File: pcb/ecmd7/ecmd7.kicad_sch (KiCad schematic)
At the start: 0 parts

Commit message: WIP: Add supply
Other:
- added sheet Supply (Supply.kicad_sch)
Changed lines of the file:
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@@
+		)
+	)
+	(sheet
+		(at 110.49 46.99)
+		(size 22.86 21.59)
+		(exclude_from_sim no)
+		(in_bom yes)
+		(on_board yes)
+		(dnp no)
+		(fields_autoplaced yes)
+		(stroke
+			(width 0.1524)
+			(type solid)
+		)
+		(fill
+			(color 0 0 0 0.0000)
+		)
+		(property "Sheetname" "Supply"
+			(at 110.49 46.2784 0)
+			(effects
+				(font
+					(size 1.27 1.27)
+				)
+				(justify left bottom)
+			)
+		)
+		(property "Sheetfile" "Supply.kicad_sch"
+			(at 110.49 69.1646 0)
+			(effects
+				(font
+					(size 1.27 1.27)
+				)
+				(justify left top)
+			)
+		)
+		(instances
+			(project "ecmd7"
+				(path "/e730e626-b0ba-4026-9c00-58e2460691fe"
+					(page "4")
+				)
+			)
 		)
 	)

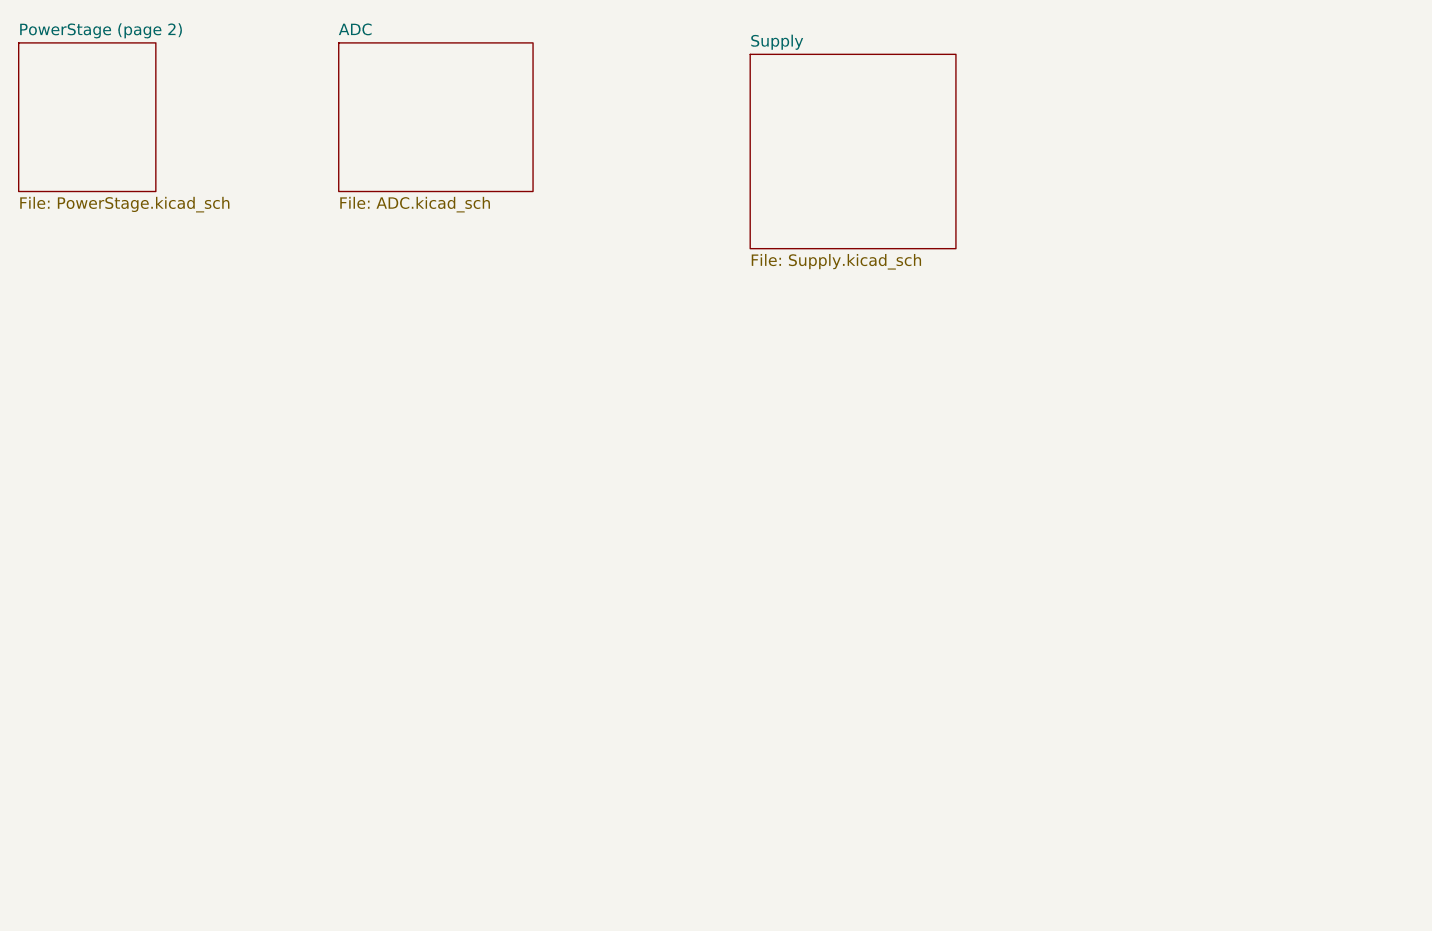
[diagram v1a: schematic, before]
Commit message: WIP: Add ADC inputs
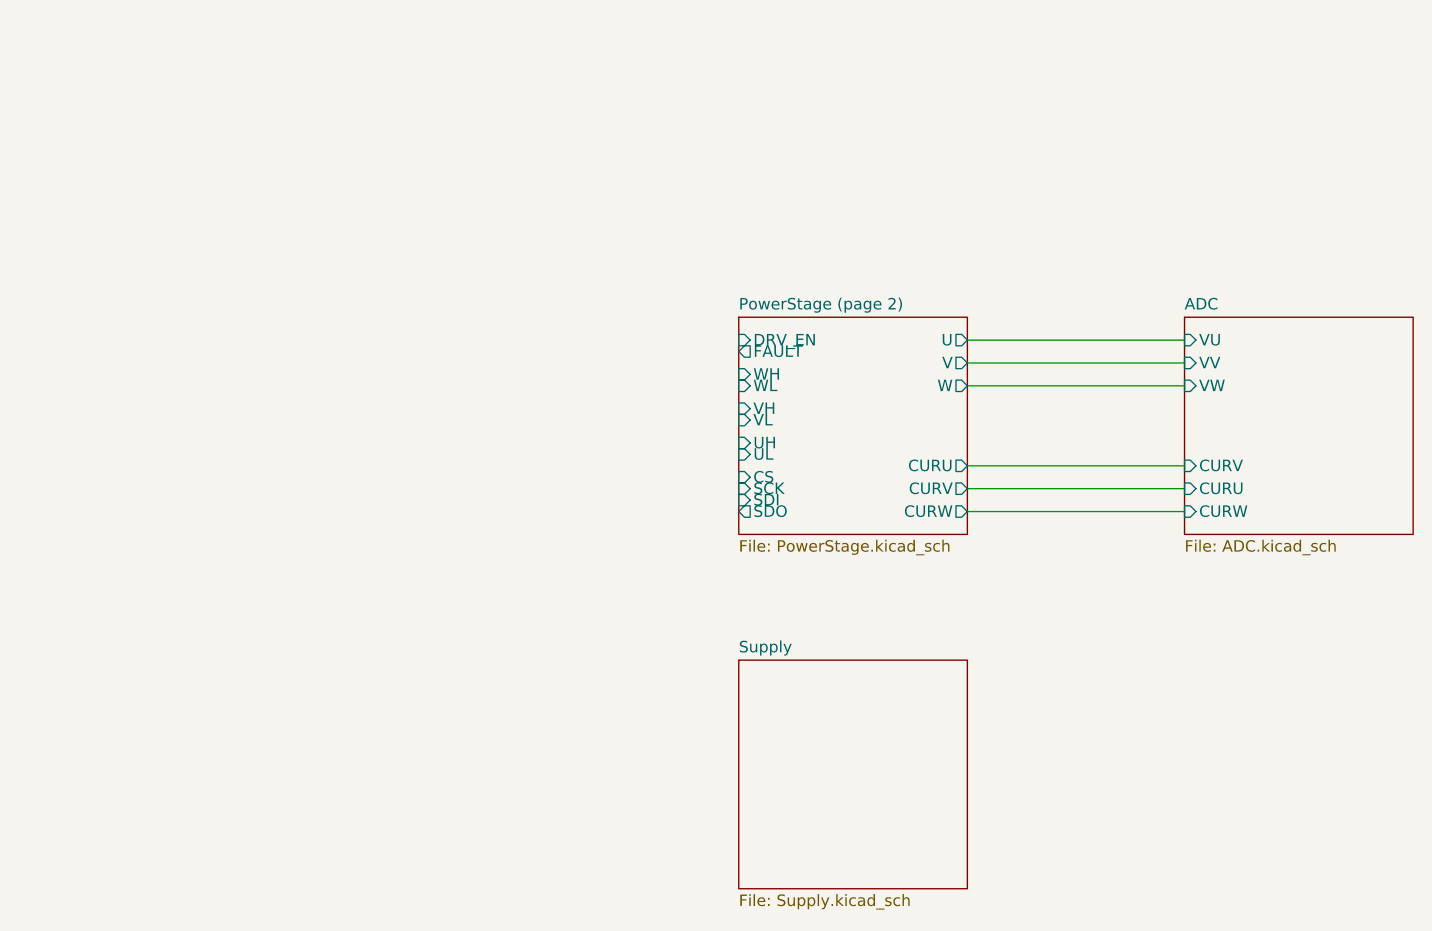
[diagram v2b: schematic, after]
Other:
- sheet ADC ports: added CURU, CURV, CURW, VU, VV, VW; removed none
- sheet PowerStage (page 2) ports: added CS, CURU, CURV, CURW, DRV_EN, FAULT, SCK, SDI, SDO, U, UH, UL, V, VH, VL, W, WH, WL; removed none

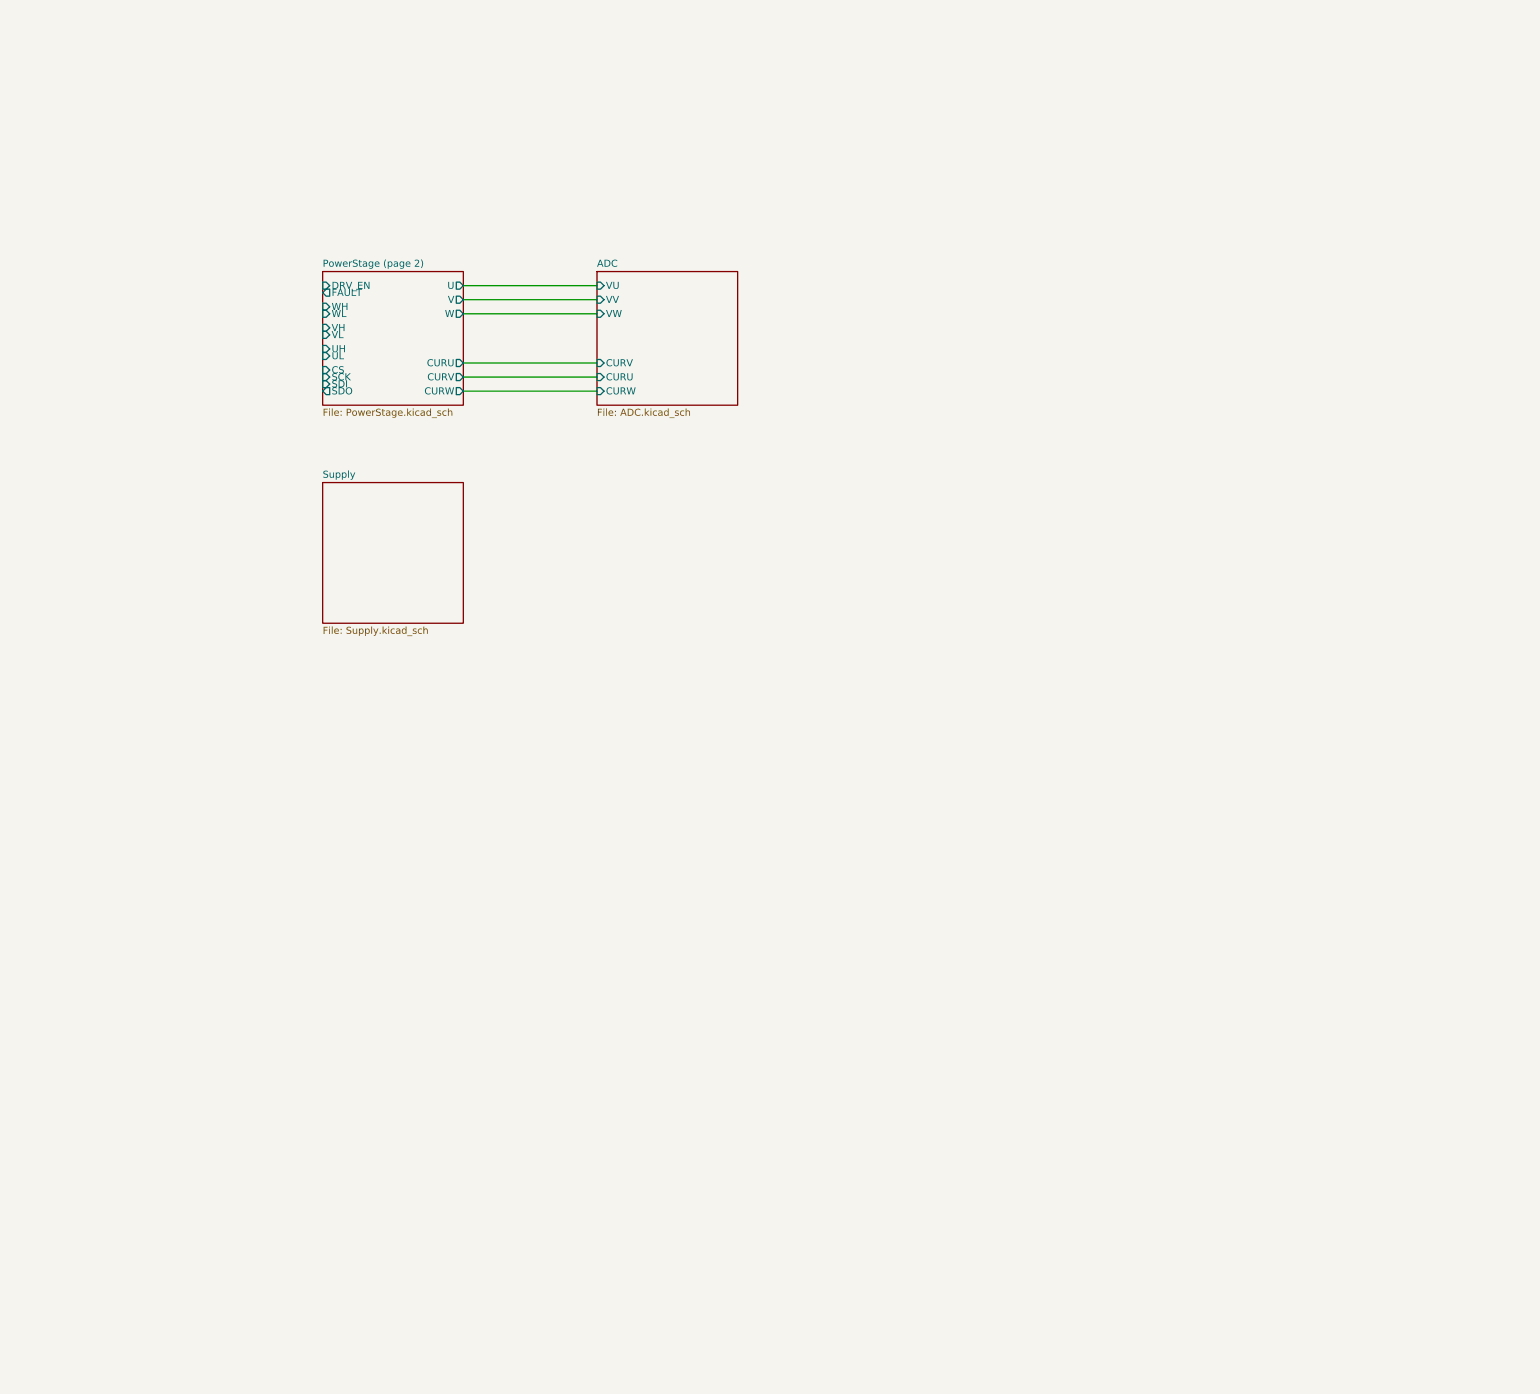
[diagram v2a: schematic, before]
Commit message: WIP: Add sensor interface Re-partition schematic
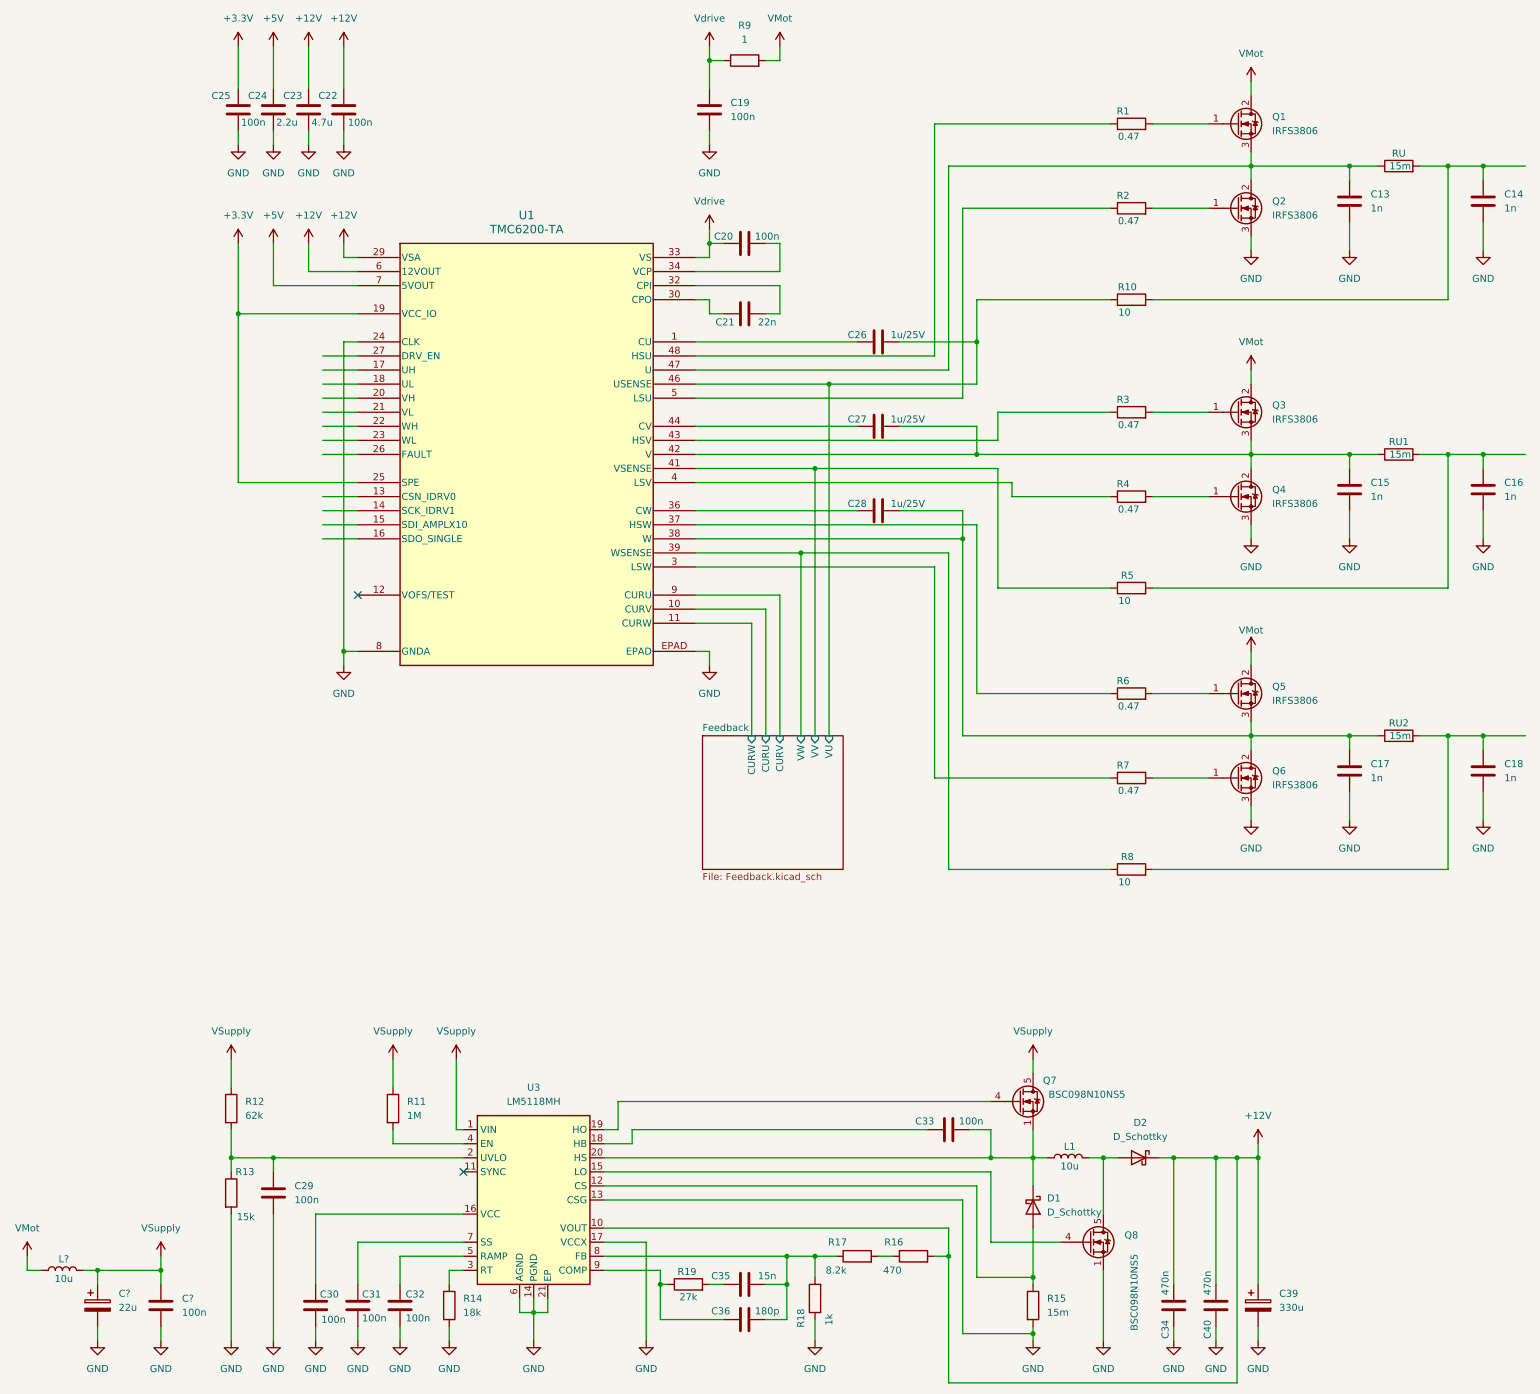
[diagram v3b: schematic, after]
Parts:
- added C13, C14, C15, C16, C17, C18: 1n, Capacitor_SMD:C_0805_2012Metric, symbol Device:C
- added C19, C20, C22, C25: 100n, Capacitor_SMD:C_0805_2012Metric, symbol Device:C
- added C21: 22n, Capacitor_SMD:C_0805_2012Metric, symbol Device:C
- added C23: 4.7u, Capacitor_SMD:C_0805_2012Metric, symbol Device:C
- added C24: 2.2u, Capacitor_SMD:C_0805_2012Metric, symbol Device:C
- added C26, C27, C28: 1u/25V, Capacitor_SMD:C_0805_2012Metric, symbol Device:C
- added C29, C30, C31, C32, C33, C?: 100n, symbol Device:C
- added C34, C40: 470n, symbol Device:C
- added C35: 15n, symbol Device:C
- added C36: 180p, symbol Device:C
- added C39: 330u, Capacitor_SMD:CP_Elec_6.3x9.9, symbol Device:C_Polarized
- added C?: 22u, Capacitor_SMD:CP_Elec_6.3x9.9, symbol Device:C_Polarized
- added D1, D2: D_Schottky, symbol Device:D_Schottky
- added L1, L?: 10u, Inductor_SMD:L_TechFuse_SL0530, symbol Device:L
- added Q1, Q2, Q3, Q4, Q5, Q6: IRFS3806, Package_TO_SOT_SMD:TO-263-2, symbol Transistor_FET:IRFS4115
- added Q7, Q8: BSC098N10NS5, Package_TO_SOT_SMD:TDSON-8-1, symbol Transistor_FET:BSC098N10NS5
- added R1, R2, R3, R4, R6, R7: 0.47, Resistor_SMD:R_0805_2012Metric, symbol Device:R
- added R10, R5, R8: 10, Resistor_SMD:R_0805_2012Metric, symbol Device:R
- added R11: 1M, Resistor_SMD:R_0805_2012Metric, symbol Device:R
- added R12: 62k, Resistor_SMD:R_0805_2012Metric, symbol Device:R
- added R13: 15k, Resistor_SMD:R_0805_2012Metric, symbol Device:R
- added R14: 18k, Resistor_SMD:R_0805_2012Metric, symbol Device:R
- added R15: 15m, symbol Device:R
- added R16: 470, Resistor_SMD:R_0805_2012Metric, symbol Device:R
- added R17: 8.2k, Resistor_SMD:R_0805_2012Metric, symbol Device:R
- added R18: 1k, Resistor_SMD:R_0805_2012Metric, symbol Device:R
- added R19: 27k, Resistor_SMD:R_0805_2012Metric, symbol Device:R
- added R9: 1, Resistor_SMD:R_0805_2012Metric, symbol Device:R
- added RU, RU1, RU2: 15m, Resistor_SMD:R_0612_1632Metric, symbol Device:R
- added U1: TMC6200-TA, eTQFP48_9x9_TRI, symbol ssta_symbols:TMC6200-TA
- added U3: LM5118MH, Package_SO:Texas_PWP0020A, symbol Regulator_Switching:LM5118MH
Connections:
- net Feedback/CURU: now also U1.10 (CURV)
- net Feedback/CURV: now also U1.9 (CURU)
- net Feedback/CURW: now also U1.11 (CURW)
- net Feedback/VU: now also C26.1, R10.1, U1.46 (USENSE)
- net Feedback/VV: now also R5.1, U1.41 (VSENSE)
- net Feedback/VW: now also R8.1, U1.39 (WSENSE)
- new net: C13.1, Q1.3 (S), Q2.2 (D), RU.1, U1.47 (U)
- new net: C35.2, C36.2, R17.1, R18.2, U3.8 (FB)
- new net: R16.1, R17.2
- new net: C29.1, R12.2, R13.1, U3.2 (UVLO)
- new net: C30.1, U3.16 (VCC)
- new net: R2.1, U1.5 (LSU)
- new net: Q2.1 (G), R2.2
- new net: C17.1, C28.1, Q5.3 (S), Q6.2 (D), RU2.1, U1.38 (W)
- new net: C18.1, R8.2, RU2.2
- new net: C36.1, R19.1, U3.9 (COMP)
- new net: D1.2 (A), R15.1, U3.12 (CS)
- new net: Q8.4 (G), U3.15 (LO)
- new net: C33.1, U3.18 (HB)
- new net: Q7.4 (G), U3.19 (HO)
- new net: C33.2, D1.1 (K), L1.1, Q7.1 (S), Q7.2 (S), Q7.3 (S), U3.20 (HS)
- new net: R14.1, U3.3 (RT)
- new net: R11.2, U3.4 (EN)
- new net: C32.1, U3.5 (RAMP)
- new net: C31.1, U3.7 (SS)
- new net: C21.1, U1.32 (CPI)
- new net: C21.2, U1.30 (CPO)
- new net: C26.2, U1.1 (CU)
- new net: C16.1, R5.2, RU1.2
- new net: C14.1, R10.2, RU.2
- new net: C35.1, R19.2
- new net: R3.1, U1.43 (HSV)
- new net: Q3.1 (G), R3.2
- new net: R7.1, U1.3 (LSW)
- new net: Q6.1 (G), R7.2
- new net: Q1.1 (G), R1.2
- new net: Q4.1 (G), R4.2
- new net: C15.1, C27.1, Q3.3 (S), Q4.2 (D), RU1.1, U1.42 (V)
- new net: D2.2 (A), L1.2, Q8.5 (D)
- new net: C20.1, U1.34 (VCP)
- new net: C28.2, U1.36 (CW)
- new net: R6.1, U1.37 (HSW)
- new net: R4.1, U1.4 (LSV)
- new net: C27.2, U1.44 (CV)
- new net: R1.1, U1.48 (HSU)
- new net: Q5.1 (G), R6.2
- new net +12V: C22.1, C23.1, C34.2, C39.1, C40.2, D2.1 (K), R16.2, U1.29 (VSA), U1.6 (12VOUT), U3.10 (VOUT)
- new net +3.3V: C25.1, U1.19 (VCC_IO), U1.25 (SPE)
- new net +5V: C24.1, U1.7 (5VOUT)
- new net GND: C13.2, C14.2, C15.2, C16.2, C17.2, C18.2, C19.2, C22.2, C23.2, C24.2, C25.2, C29.2, C30.2, C31.2, C32.2, C34.1, C39.2, C40.1, C?.2, C?.2, Q2.3 (S), Q4.3 (S), Q6.3 (S), Q8.1 (S), Q8.2 (S), Q8.3 (S), R13.2, R14.2, R15.2, R18.1, U1.24 (CLK), U1.8 (GNDA), U1.EPAD, U3.13 (CSG), U3.14 (PGND), U3.17 (VCCX), U3.21 (EP), U3.6 (AGND)
- new net VMot: L?.1, Q1.2 (D), Q3.2 (D), Q5.2 (D), R9.2
- new net VSupply: C?.1, C?.1, L?.2, Q7.5 (D), R11.1, R12.1, U3.1 (VIN)
- new net Vdrive: C19.1, C20.2, R9.1, U1.33 (VS)
- no-connect marks 0 -> 2
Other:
- sheet ADC renamed Feedback
- removed sheet PowerStage (page 2)
- removed sheet Supply
- sheet Feedback: file ADC.kicad_sch -> Feedback.kicad_sch
- title: (none) -> ECMD7 Power Converter

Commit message: Finlize schematics
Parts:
- added J1, J2, J3: Conn_02x06_Odd_Even, Connector_PinHeader_1.27mm:PinHeader_2x06_P1.27mm_Horizontal, symbol Connector_Generic:Conn_02x06_Odd_Even
- added J4: Conn_01x02_Socket, Connector_AMASS:AMASS_XT60-F_1x02_P7.20mm_Vertical, symbol Connector:Conn_01x02_Socket
- added J5: DE9_Socket, symbol Connector:DE9_Socket
- added J6: Conn_01x04_Socket, Connector_PinHeader_1.27mm:PinHeader_1x04_P1.27mm_Vertical, symbol Connector:Conn_01x04_Socket
- added JU1, JV1, JW1: Screw_Terminal_01x01, MountingHole:MountingHole_3.2mm_M3_Pad_TopBottom, symbol Connector:Screw_Terminal_01x01
- added R44, R45: 4.7k, Resistor_SMD:R_0805_2012Metric, symbol Device:R
- gave numbers to parts that had none: 3
- renumbered RU to RU3
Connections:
- net +12V: now also J5.4
- net +3.3V: now also J1.1 (Pin_1), J1.2 (Pin_2), J2.1 (Pin_1), J2.2 (Pin_2), J3.1 (Pin_1), J3.2 (Pin_2), J6.2 (Pin_2), R44.1, R45.1
- net GND: now also J1.3 (Pin_3), J1.4 (Pin_4), J2.3 (Pin_3), J2.4 (Pin_4), J3.3 (Pin_3), J3.4 (Pin_4), J4.2 (Pin_2), J5.5, J6.1 (Pin_1)
- net VMot: now also J4.1 (Pin_1)
- net at C18.1, R8.2, RU2.2: now also JW1.1 (Pin_1)
- net at C16.1, R5.2, RU1.2: now also JV1.1 (Pin_1)
- net at C14.1, R10.2, RU3.2: now also JU1.1 (Pin_1)
- net CS_DRV: now reaches U1.13 (CSN_IDRV0)
- net CS_DRV: now also J2.10 (Pin_10)
- net SPI_SCK: now reaches U1.14 (SCK_IDRV1)
- net SPI_SCK: now also J2.9 (Pin_9)
- net SPI_SDI: now reaches U1.15 (SDI_AMPLX10)
- net SPI_SDI: now also J2.11 (Pin_11)
- net SPI_SDO: now reaches U1.16 (SDO_SINGLE)
- net SPI_SDO: now also J2.12 (Pin_12)
- net UH: now reaches U1.17 (UH)
- net UH: now also J1.10 (Pin_10)
- net UL: now reaches U1.18 (UL)
- net UL: now also J1.9 (Pin_9)
- net VH: now reaches U1.20 (VH)
- net VH: now also J1.8 (Pin_8)
- net VL: now reaches U1.21 (VL)
- net VL: now also J1.7 (Pin_7)
- net WH: now reaches U1.22 (WH)
- net WH: now also J1.6 (Pin_6)
- net WL: now reaches U1.23 (WL)
- net WL: now also J1.5 (Pin_5)
- net FAULT: now reaches U1.26 (FAULT)
- net FAULT: now also J1.12 (Pin_12)
- net DRV_EN: now reaches U1.27 (DRV_EN)
- net DRV_EN: now also J1.11 (Pin_11)
- net Feedback/CURU renamed I_V
- net Feedback/CURV renamed I_U
- net Feedback/CURW renamed I_W
- net Feedback/VU: no longer names the net of C26.1, R10.1, U1.46 (USENSE)
- net Feedback/VV: no longer names the net of R5.1, U1.41 (VSENSE)
- net Feedback/VW: no longer names the net of R8.1, U1.39 (WSENSE)
- new net AD_SCK: J3.12 (Pin_12)
- new net AD_SDO_IU: J3.9 (Pin_9)
- new net AD_SDO_IV: J3.10 (Pin_10)
- new net AD_SDO_IW: J3.7 (Pin_7)
- new net AD_SDO_VBUS: J3.8 (Pin_8)
- new net CS_AD: J3.11 (Pin_11)
- new net CS_EXT: J2.7 (Pin_7)
- new net ENC_A: J2.5 (Pin_5)
- new net ENC_AN: J5.6
- new net ENC_AP: J5.1
- new net ENC_B: J2.6 (Pin_6)
- new net ENC_BN: J5.7
- new net ENC_BP: J5.2
- new net ENC_Z: J2.8 (Pin_8)
- new net ENC_ZN: J5.8
- new net ENC_ZP: J5.3
- new net I2C_SCL: J3.6 (Pin_6), J6.4 (Pin_4), R45.2
- new net I2C_SDA: J3.5 (Pin_5), J6.3 (Pin_3), R44.2
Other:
- sheet Feedback ports: added none; removed CURU, CURV, CURW, VU, VV, VW
- moved on the sheet: C13, C14, C15, C16, C17, C18, C19, C20, C21, C22, C23, C24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
